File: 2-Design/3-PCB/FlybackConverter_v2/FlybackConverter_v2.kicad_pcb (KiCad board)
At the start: 2 copper layers, 120 x 40 mm, 56 parts, among them U1 TL431DBV, U2 LM7812_TO220

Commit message: I guess, only last edits left for PCB design.
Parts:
- moved CSnubber1 8.45 mm to (111.1, 27.3)
- moved RSnubber1 8.36 mm to (111.5, 31.2)
- moved DSnubber1 4.92 mm to (104.1, 26.6)
- moved CIN2 1.58 mm to (43.7, 22.9)
- moved CIN3 1.43 mm to (47.0, 22.8)
- moved CIN1 1.33 mm to (56.2, 21.8)
- moved CIN4 1.33 mm to (50.3, 22.8)
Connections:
- INPUT1 pad 1: GND -> Net-(CIN1-Pad1)
- INPUT1 pad 2: Net-(CIN1-Pad1) -> GND
- TR1 pad 11: Net-(CIN1-Pad1) -> (no net)
- TR1 pad 7: (no net) -> Net-(DSnubber1-Pad2)
- TR1 pad 8: Net-(DSnubber1-Pad2) -> (no net)
- TR1 pad 9: (no net) -> Net-(CIN1-Pad1)
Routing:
- net GND: track 89.7 -> 104.0 mm
- net Net-(CIN1-Pad1): track 0.00 -> 13.8 mm
- added copper zone on B.Cu, net GND
- added copper zone on F.Cu, net GND
- added copper zone on F.Cu, net Net-(CIN1-Pad1)
- added copper zone on B.Cu, net Net-(CSnubber1-Pad2)
- added copper zone on F.Cu, net Net-(CSnubber1-Pad2)
- added copper zone on B.Cu, net Net-(DSnubber1-Pad2)
- added copper zone on F.Cu, net Net-(DSnubber1-Pad2)
- added copper zone on B.Cu, net Net-(MOSFET1-Pad1)

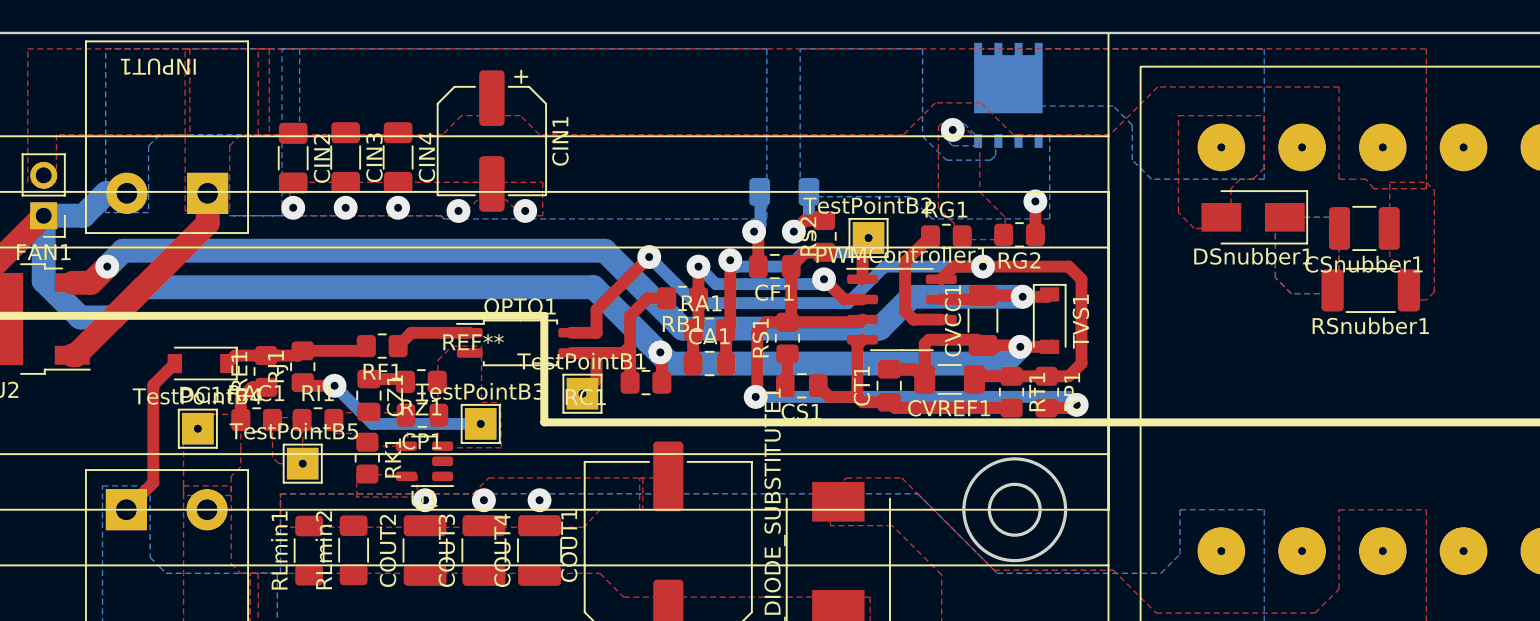
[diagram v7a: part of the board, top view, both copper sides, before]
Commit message: Gate loop is too long :'(. I_sense capacitor should also be placed closer to the IC.
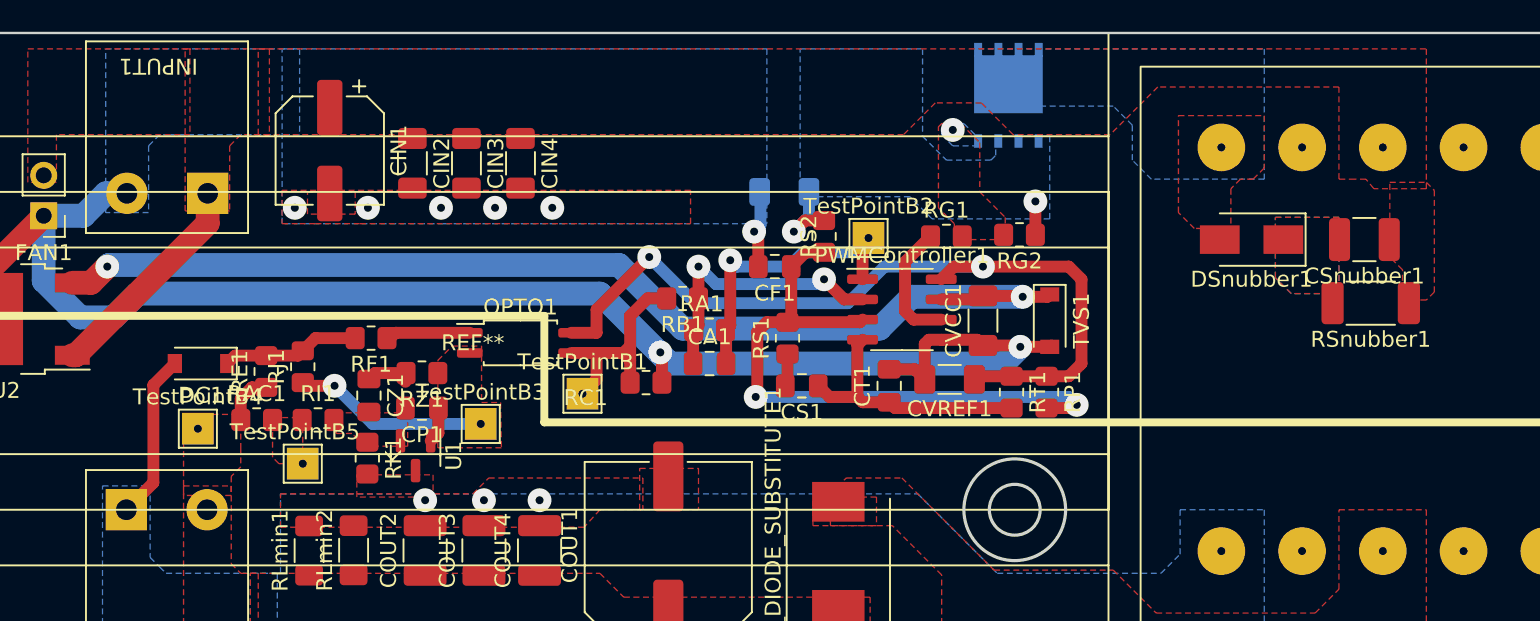
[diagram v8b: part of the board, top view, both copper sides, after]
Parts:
- U1: value TL431DBV -> TL431DBZ; footprint Package_TO_SOT_SMD:SOT-23-5 -> Package_TO_SOT_SMD:SOT-23
- moved CIN1 10.2 mm to (46.0, 22.4)
- moved CIN4 7.71 mm to (58.0, 23.2)
- moved CIN3 7.61 mm to (54.6, 23.2)
- moved CIN2 7.51 mm to (51.2, 23.2)
- moved DSnubber1 1.40 mm to (104.0, 28.0)
- moved RF1 0.86 mm to (48.6, 34.2)
- moved RSnubber1 0.80 mm to (111.5, 32.0)
- moved CSnubber1 0.70 mm to (111.1, 28.0)
- moved U1 0.66 mm to (51.4, 41.6), turned to -90 degrees
- moved RZ1 0.55 mm to (51.8, 36.4)
- moved CP1 0.45 mm to (51.8, 38.6)
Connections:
- U1 pad 1: (no net) -> Net-(CP1-Pad1)
- U1 pad 2: (no net) -> Net-(CP1-Pad2)
- U1 pad 3: Net-(CP1-Pad1) -> GNDREF
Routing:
- net Net-(CP1-Pad1): track 12.8 -> 15.1 mm
- net Net-(CVCC1-Pad2): track 70.5 -> 69.8 mm
